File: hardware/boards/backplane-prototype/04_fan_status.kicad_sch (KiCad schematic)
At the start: 14 parts, among them J11 12V 3-WIRE FAN, J12 DS18B20 EXT SUPPLY, J9 12V 3-WIRE FAN, Q1 AO3407A, Q2 2N7002, Q3 AO3407A, Q4 2N7002

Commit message: checkpoint: save fan schematic layout
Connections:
- net FAN_GATE: no longer names the net of Q1.1 (G), Q2.3 (D), R18.2
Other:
- note added: "NOTES: - J9 and J11 support 3-wire fans only: pin 1 GND pin 2 independently switched +12 V pin 3 open-collector tach. - Q1/Q2 and Q3/Q4 implement high-side supply PWM; TODO: - [ ] validate PWM, startup, stall, tach, and combined 12 V rail loading"
- note removed: "J9 and J11 support 3-wire fans only: pin 1 GND, pin 2 independently switched +12 V, pin 3 open-collector tach. Q1/Q2 and Q3/Q4 implement high-side supply PWM; validate PWM, startup, stall, tach, and combined 12 V rail loading on first articles."
- moved on the sheet: J9, Q1, Q2, R18, R19, R20

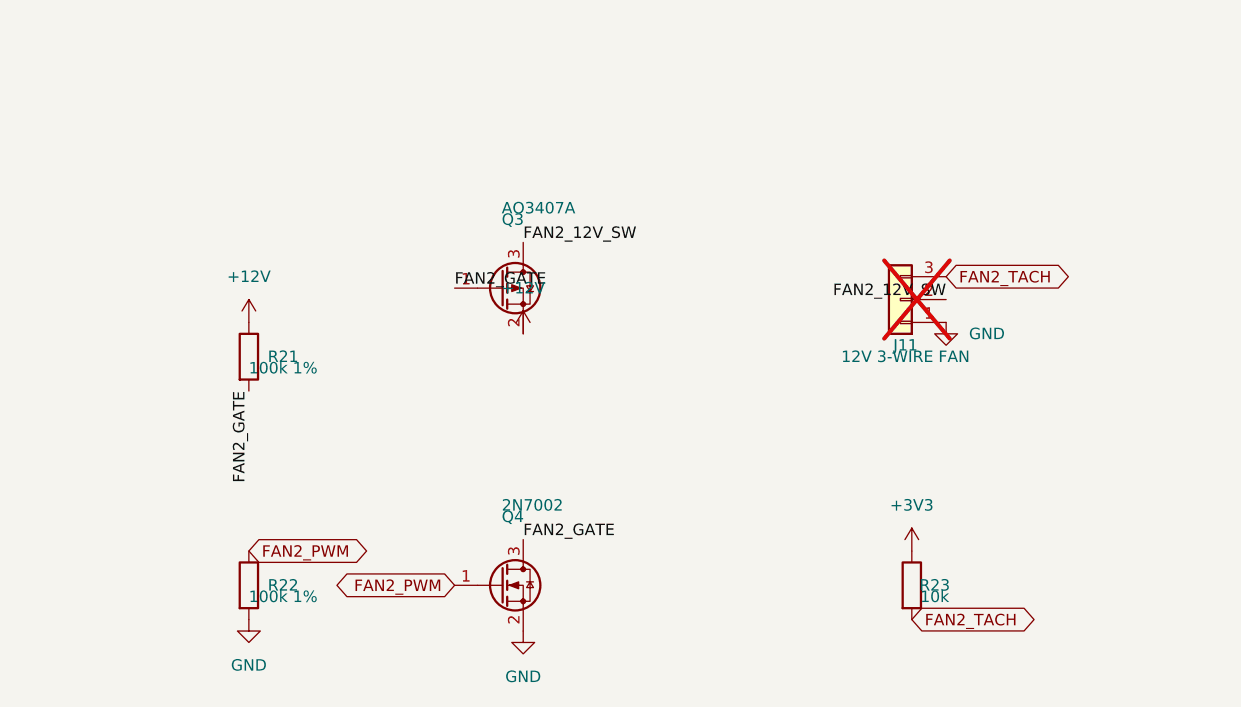
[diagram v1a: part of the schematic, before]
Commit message: Match second fan channel schematic layout
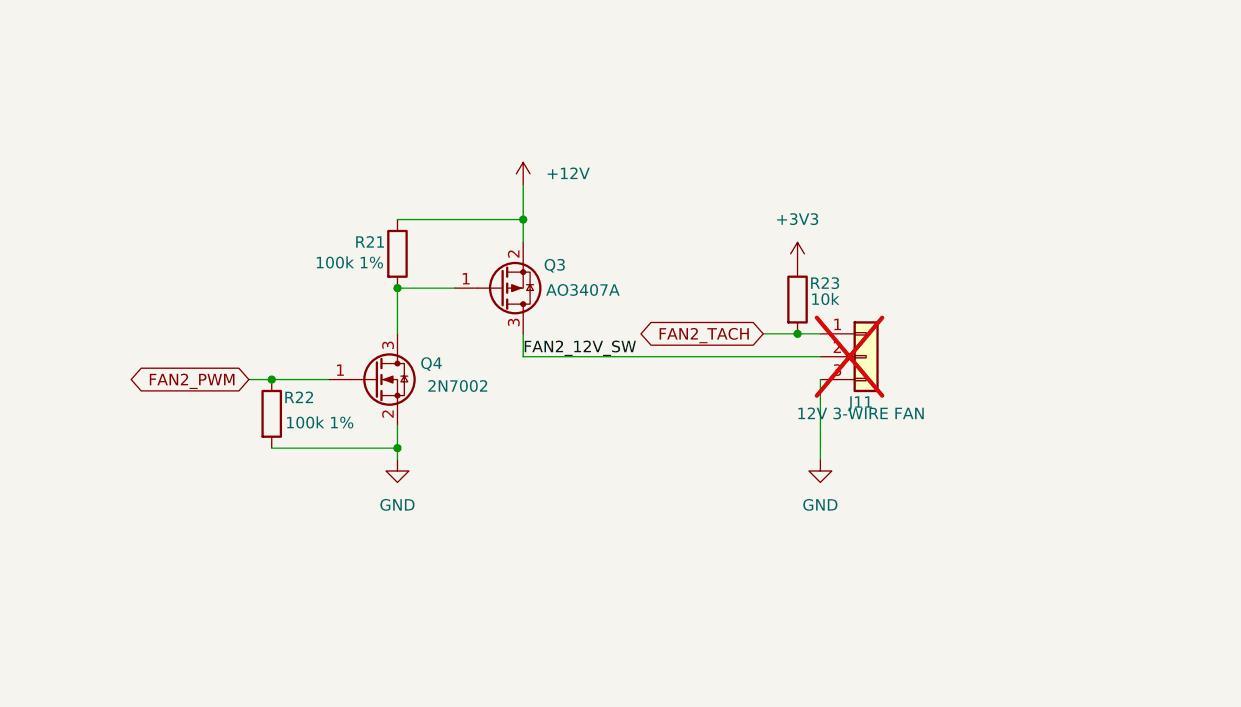
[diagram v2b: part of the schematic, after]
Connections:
- net FAN2_TACH: now also J11.1 (Pin_1); no longer J11.3 (Pin_3)
- net GND: now also J11.3 (Pin_3); no longer J11.1 (Pin_1)
- net FAN2_GATE: no longer names the net of Q3.1 (G), Q4.3 (D), R21.2
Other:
- moved on the sheet: J11, Q4, R21, R22, R23

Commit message: checkpoint: save fan and buck schematic edits
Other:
- note added: "NOTES: - J9 and J11 support 3-wire fans only: 1 GND 2 independently switched +12 V 3 open-collector tach. - Q1/Q2 and Q3/Q4 implement high-side supply PWM - J12: External DS18B20 temp probe; with 4.7k pullup on data 1 GND 2 DQ 3 +3V3 TODO: - [ ] validate PWM, startup, stall, tach, and combined 12 V rail loading"
- note removed: "J12: DS18B20 external supply, 1=GND, 2=DQ, 3=+3V3; R24=4.7 kOhm DQ pull-up."
- note removed: "NOTES: - J9 and J11 support 3-wire fans only: pin 1 GND pin 2 independently switched +12 V pin 3 open-collector tach. - Q1/Q2 and Q3/Q4 implement high-side supply PWM; TODO: - [ ] validate PWM, startup, stall, tach, and combined 12 V rail loading"
- moved on the sheet: J11, J12, J9, Q1, Q2, Q3, Q4, R18, R19, R20, R21, R22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

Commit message: checkpoint: save latest backplane routing
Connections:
- net FAN2_TACH: now also J11.3 (Pin_3); no longer J11.1 (Pin_1)
- net GND: now also J11.1 (Pin_1); no longer J11.3 (Pin_3)
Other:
- moved on the sheet: J12, R24
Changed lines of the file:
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@@
 	)
 	(junction
-		(at 233.68 72.39)
+		(at 246.38 72.39)
 		(diameter 0)
 		(color 0 0 0 0)
@@
 	)
 	(junction
-		(at 242.57 80.01)
+		(at 237.49 80.01)
 		(diameter 0)
 		(color 0 0 0 0)
@@
 	(wire
 		(pts
-			(xy 252.73 80.01) (xy 242.57 80.01)
-		)
-		(stroke
-			(width 0)
-			(type default)
-		)
-	)
-	(wire
-		(pts
-			(xy 233.68 72.39) (xy 242.57 72.39)
+			(xy 227.33 80.01) (xy 237.49 80.01)
+		)
+		(stroke
+			(width 0)
+			(type default)
+		)
+	)
+	(wire
+		(pts
+			(xy 246.38 72.39) (xy 237.49 72.39)
 		)
 		(stroke
@@
 	(wire
 		(pts
-			(xy 233.68 72.39) (xy 233.68 77.47)
-		)
-		(stroke
-			(width 0)
-			(type default)
-		)
-	)
-	(wire
-		(pts
-			(xy 242.57 80.01) (xy 233.68 80.01)
+			(xy 246.38 72.39) (xy 246.38 77.47)
+		)
+		(stroke
+			(width 0)
+			(type default)
+		)
+	)
+	(wire
+		(pts
+			(xy 237.49 80.01) (xy 246.38 80.01)
 		)
 		(stroke
@@
 	(global_label "DS18B20_DATA"
 		(shape bidirectional)
-		(at 252.73 80.01 0)
+		(at 227.33 80.01 180)
 		(effects
 			(font
 				(size 1.27 1.27)
 			)
-			(justify left)
+			(justify right)
 		)
 		(property "Intersheetrefs" "${INTERSHEET_REFS}"
-			(at 252.73 80.01 0)
+			(at 227.33 80.01 0)
 			(hide yes)
 			(show_name no)
@@
 		(lib_id "Connector_Generic:Conn_01x03")
 		(at 198.12 78.74 0)
+		(mirror x)
 		(unit 1)
 		(body_style 1)
@@
 		(dnp yes)
 		(property "Reference" "J11"
-			(at 197.55 83.82 0)
+			(at 197.55 73.66 0)
 			(show_name no)
 			(do_not_autoplace no)
@@
 		)
 		(property "Value" "12V 3-WIRE FAN"
-			(at 197.55 85.09 0)
+			(at 197.55 72.39 0)
+			(hide yes)
 			(show_name no)
 			(do_not_autoplace no)
@@
 		)
 		(property "Footprint" "Connector_MiniRackPower:FanPinHeader_1x03_P2.54mm_Vertical_JLC_Edge"
-			(at 202.5 72.08 0)
+			(at 202.5 85.4 0)
 			(hide yes)
 			(show_name no)
@@
 		)
 		(property "Datasheet" ""
-			(at 202.5 72.08 0)
+			(at 202.5 85.4 0)
 			(hide yes)
 			(show_name no)
@@
 		)
 		(property "Description" "Generic connector, single row, 01x03, script generated (kicad-library-utils/schlib/autogen/connector/)"
-			(at 202.5 72.08 0)
+			(at 202.5 85.4 0)
 			(hide yes)
 			(show_name no)
@@
 		)
 		(property "MPN" "TBD / user fan header"
-			(at 202.5 72.08 0)
+			(at 202.5 85.4 0)
 			(hide yes)
 			(show_name no)
@@
 		)
 		(property "Manufacturer" "TBD"
-			(at 202.5 72.08 0)
+			(at 202.5 85.4 0)
 			(hide yes)
 			(show_name no)
@@
 		)
 		(property "LCSC" ""
-			(at 202.5 72.08 0)
+			(at 202.5 85.4 0)
 			(hide yes)
 			(show_name no)
@@
 		)
 		(property "Package" "1x3 2.54 mm fan header"
-			(at 202.5 72.08 0)
+			(at 202.5 85.4 0)
 			(hide yes)
 			(show_name no)
@@
 	(symbol
 		(lib_id "Device:R")
-		(at 242.57 76.2 0)
+		(at 237.49 76.2 0)
+		(mirror y)
 		(unit 1)
 		(body_style 1)
@@
 		(dnp no)
 		(property "Reference" "R24"
-			(at 245.618 74.676 0)
+			(at 234.442 74.676 0)
 			(show_name no)
 			(do_not_autoplace no)
@@
 		)
 		(property "Value" "4.7k 1%"
-			(at 247.65 77.47 0)
+			(at 232.41 77.47 0)
 			(show_name no)
 			(do_not_autoplace no)
@@
 		)
 		(property "Footprint" "Resistor_SMD:R_0603_1608Metric"
-			(at 240.222 76.07 90)
+			(at 239.838 76.07 90)
 			(hide yes)
 			(show_name no)
@@
 		)
 		(property "Datasheet" ""
-			(at 242 76.07 0)
+			(at 238.06 76.07 0)
 			(hide yes)
 			(show_name no)
@@
 		)
 		(property "Description" ""
-			(at 242 76.07 0)
+			(at 238.06 76.07 0)
 			(hide yes)
 			(show_name no)
@@
 		)
 		(property "MPN" "0603WAF4701T5E"
-			(at 242 76.07 0)
+			(at 238.06 76.07 0)
 			(hide yes)
 			(show_name no)
@@
 		)
 		(property "Manufacturer" "UNI-ROYAL (Uniroyal Elec)"
-			(at 242 76.07 0)
+			(at 238.06 76.07 0)
 			(hide yes)
 			(show_name no)
@@
 		)
 		(property "LCSC" "C23162"
-			(at 242 76.07 0)
+			(at 238.06 76.07 0)
 			(hide yes)
 			(show_name no)
@@
 		)
 		(property "Tolerance" "1%"
-			(at 242 76.07 0)
+			(at 238.06 76.07 0)
 			(hide yes)
 			(show_name no)
@@
 	(symbol
 		(lib_id "Connector_Generic:Conn_01x03")
-		(at 228.6 80.01 180)
+		(at 251.46 80.01 0)
+		(mirror x)
 		(unit 1)
 		(body_style 1)
@@
 		(dnp yes)
 		(property "Reference" "J12"
-			(at 229.17 85.09 0)
+			(at 250.89 85.09 0)
 			(show_name no)
 			(do_not_autoplace no)
@@
 		)
 		(property "Value" "DS18B20 EXT SUPPLY"
-			(at 224.79 87.884 0)
+			(at 255.27 87.884 0)
 			(hide yes)
 			(show_name no)
@@
 		)
 		(property "Footprint" "Connector_PinHeader_2.54mm:PinHeader_1x03_P2.54mm_Vertical"
-			(at 229.17 79.7 0)
+			(at 250.89 79.7 0)
 			(hide yes)
 			(show_name no)
@@
 		)
 		(property "Datasheet" ""
-			(at 229.17 79.7 0)
+			(at 250.89 79.7 0)
 			(hide yes)
 			(show_name no)
@@
 		)
 		(property "Description" "Generic connector, single row, 01x03, script generated (kicad-library-utils/schlib/autogen/connector/)"
-			(at 229.17 79.7 0)
+			(at 250.89 79.7 0)
 			(hide yes)
 			(show_name no)
@@
 		)
 		(property "MPN" "TBD / user pin header"
-			(at 229.17 79.7 0)
+			(at 250.89 79.7 0)
 			(hide yes)
 			(show_name no)
@@
 		)
 		(property "Manufacturer" "TBD"
-			(at 229.17 79.7 0)
+			(at 250.89 79.7 0)
 			(hide yes)
 			(show_name no)
@@
 		)
 		(property "LCSC" ""
-			(at 229.17 79.7 0)
+			(at 250.89 79.7 0)
 			(hide yes)
 			(show_name no)
@@
 		)
 		(property "Package" "1x3 2.54 mm pin header"
-			(at 229.17 79.7 0)
+			(at 250.89 79.7 0)
 			(hide yes)
 			(show_name no)
@@
 	(symbol
 		(lib_id "power:+3V3")
-		(at 233.68 72.39 0)
+		(at 246.38 72.39 0)
+		(mirror y)
 		(unit 1)
 		(body_style 1)
@@
 		(fields_autoplaced yes)
 		(property "Reference" "#PWR01"
-			(at 233.68 76.2 0)
+			(at 246.38 76.2 0)
 			(hide yes)
 			(show_name no)
@@
 		)
 		(property "Value" "+3V3"
-			(at 233.68 67.31 0)
+			(at 246.38 67.31 0)
 			(show_name no)
 			(do_not_autoplace no)
@@
 		)
 		(property "Footprint" ""
-			(at 233.68 72.39 0)
+			(at 246.38 72.39 0)
 			(hide yes)
 			(show_name no)
@@
 		)
 		(property "Datasheet" ""
-			(at 233.68 72.39 0)
+			(at 246.38 72.39 0)
 			(hide yes)
 			(show_name no)
@@
 		)
 		(property "Description" "Power symbol creates a global label with name \"+3V3\""
-			(at 233.68 72.39 0)
+			(at 246.38 72.39 0)
 			(hide yes)
 			(show_name no)
@@
 	(symbol
 		(lib_id "power:GND")
-		(at 233.68 82.55 0)
+		(at 246.38 82.55 0)
+		(mirror y)
 		(unit 1)
 		(body_style 1)
@@
 		(fields_autoplaced yes)
 		(property "Reference" "#PWR02"
-			(at 233.68 88.9 0)
+			(at 246.38 88.9 0)
 			(hide yes)
 			(show_name no)
@@
 		)
 		(property "Value" "GND"
-			(at 233.68 87.63 0)
+			(at 246.38 87.63 0)
 			(show_name no)
 			(do_not_autoplace no)
@@
 		)
 		(property "Footprint" ""
-			(at 233.68 82.55 0)
+			(at 246.38 82.55 0)
 			(hide yes)
 			(show_name no)
@@
 		)
 		(property "Datasheet" ""
-			(at 233.68 82.55 0)
+			(at 246.38 82.55 0)
 			(hide yes)
 			(show_name no)
@@
 		)
 		(property "Description" "Power symbol creates a global label with name \"GND\" , ground"
-			(at 233.68 82.55 0)
-			(hide yes)
-			(show_name no)
+			(at 246.38 82.55 0)
+			(hide yes)
+			(show_name no)
